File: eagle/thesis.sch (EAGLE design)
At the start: 13 parts

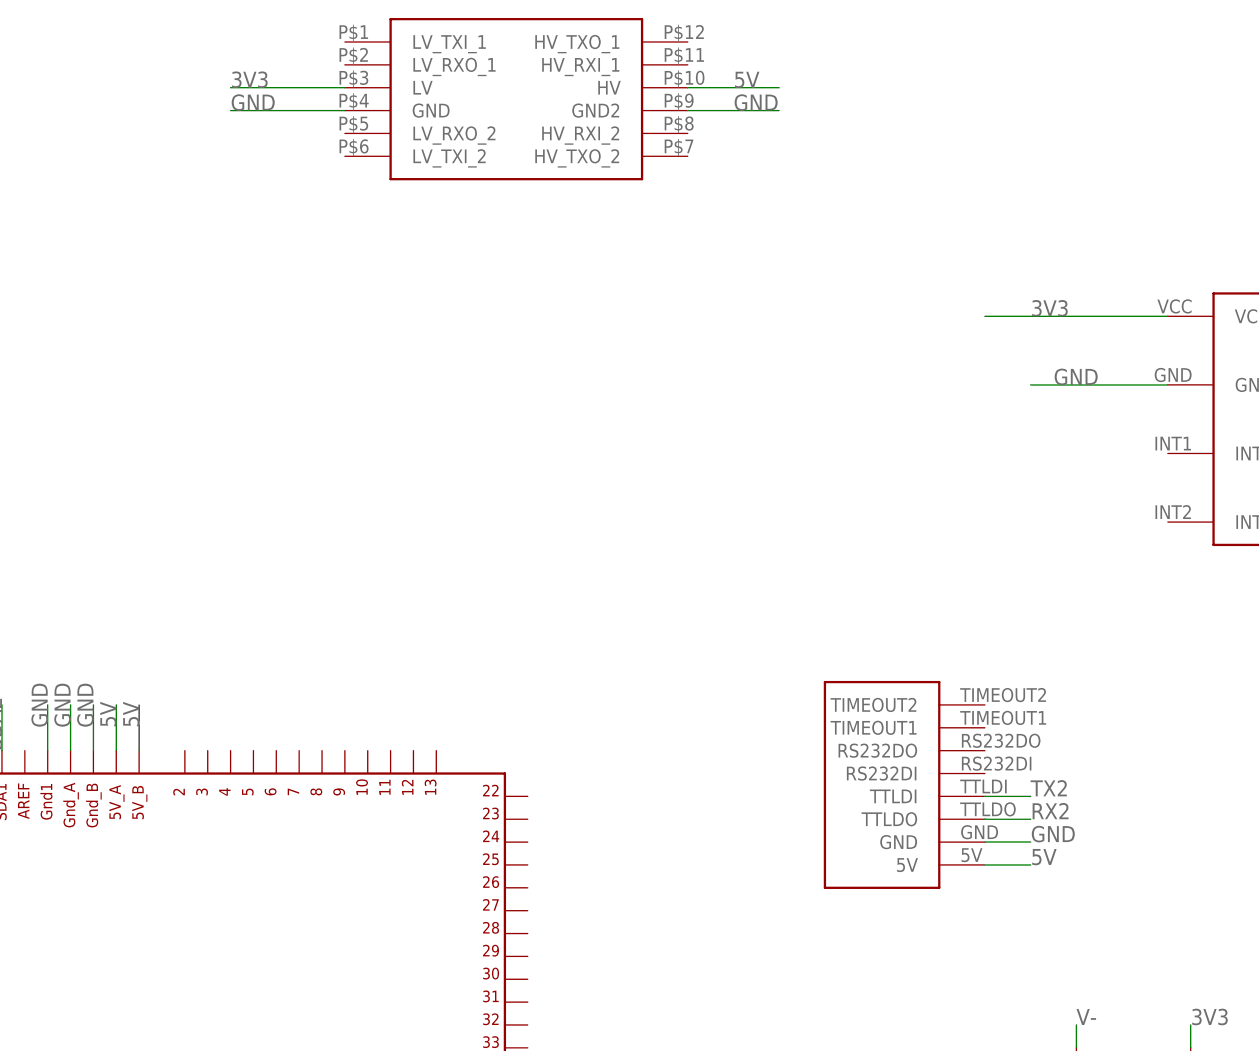
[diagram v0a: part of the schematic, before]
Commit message: added smaller satellite board
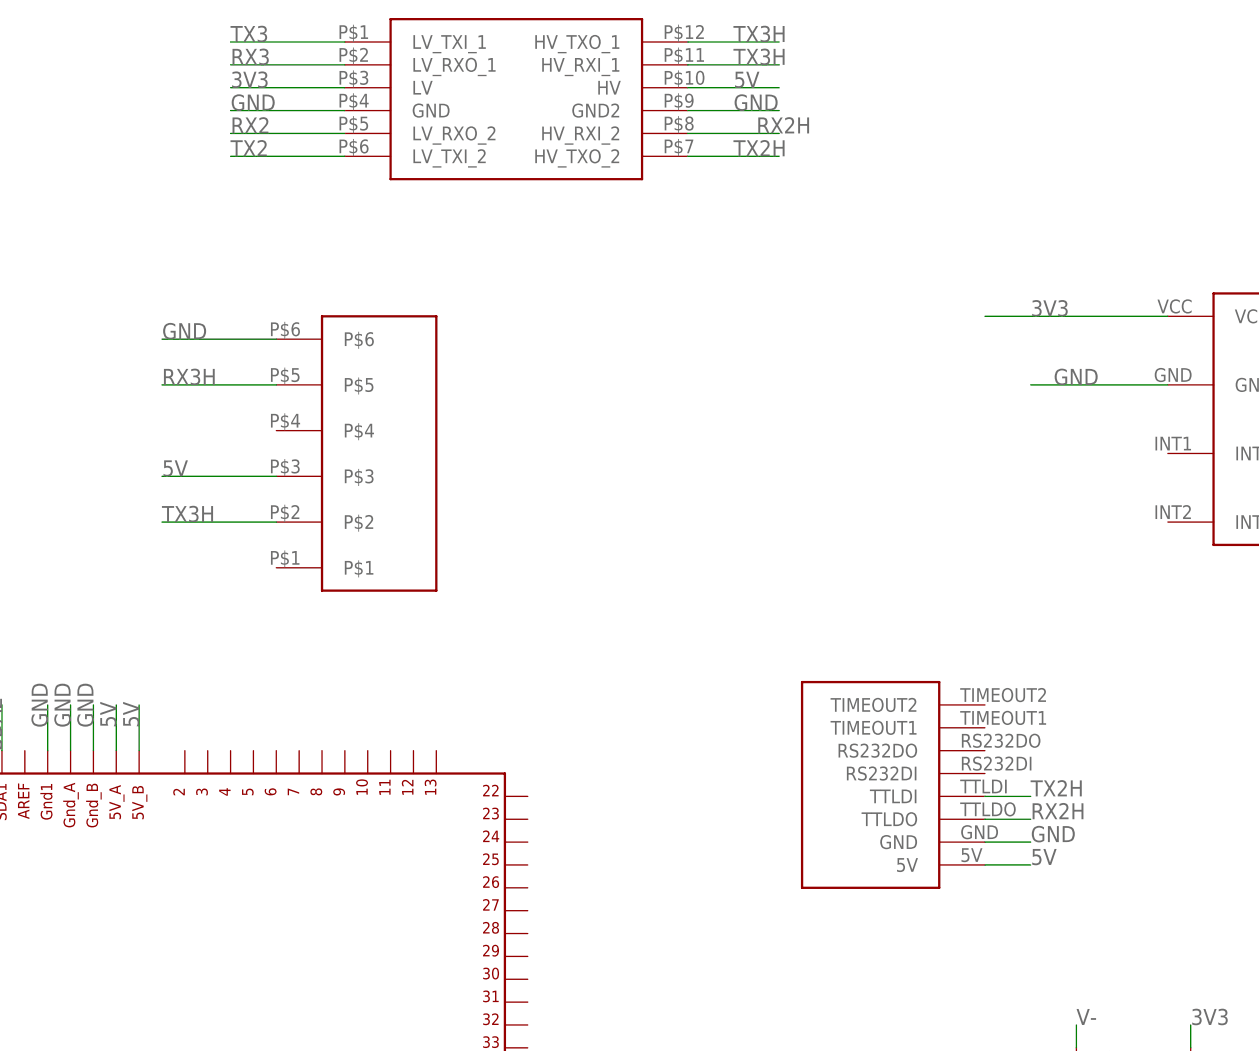
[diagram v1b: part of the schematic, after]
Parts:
- added U$8: RJ11V, RJ11V:RJ11V
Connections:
- new net RX2H: U$2.HV_RXI_2, U$6.TTLDO
- new net RX3H: U$8.P$5
- new net TX2H: U$2.HV_TXO_2, U$6.TTLDI
- new net TX3H: U$2.HV_RXI_1, U$2.HV_TXO_1, U$8.P$2
- net 5V: now also U$8.P$3
- net GND: now also U$8.P$6
- net RX2: now also U$2.LV_RXO_2; no longer U$6.TTLDO
- net RX3: now also U$2.LV_RXO_1
- net TX2: now also U$2.LV_TXI_2; no longer U$6.TTLDI
- net TX3: now also U$2.LV_TXI_1

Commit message: routed thesis board
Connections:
- new net D52: U$1.52
- new net D53: U$1.53
- net ACCELCS: now also U$1.8; no longer U$1.53
- net GND: no longer U$1.GND_DEBUG
- net RX3H: now also U$2.HV_RXI_1
- net SDCS: now also U$1.9; no longer U$1.52
- net TX3H: no longer U$2.HV_RXI_1
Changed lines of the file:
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@@
-</segment>
-<segment>
-<pinref part="U$1" gate="G$1" pin="GND_DEBUG"/>
-<wire x1="-2.54" y1="25.4" x2="-10.16" y2="25.4" width="0.1524" layer="91"/>
-<label x="-10.16" y="25.4" size="1.778" layer="95"/>
 </segment>
 <segment>
@@
 </segment>
 <segment>
+<pinref part="U$1" gate="G$1" pin="9"/>
+<wire x1="48.26" y1="93.98" x2="48.26" y2="86.36" width="0.1524" layer="91"/>
+<label x="48.26" y="88.9" size="1.778" layer="95" rot="R90"/>
+</segment>
+</net>
+<net name="ACCELCS" class="0">
+<segment>
+<pinref part="U$4" gate="G$1" pin="CS"/>
+<wire x1="200.66" y1="111.76" x2="180.34" y2="111.76" width="0.1524" layer="91"/>
+<label x="190.5" y="111.76" size="1.778" layer="95"/>
+</segment>
+<segment>
+<pinref part="U$1" gate="G$1" pin="8"/>
+<wire x1="45.72" y1="86.36" x2="45.72" y2="93.98" width="0.1524" layer="91"/>
+<label x="45.72" y="88.9" size="1.778" layer="95" rot="R90"/>
+</segment>
+</net>
+<net name="SDA2" class="0">
+<segment>
+<pinref part="U$1" gate="G$1" pin="SDA1"/>
+<wire x1="10.16" y1="86.36" x2="10.16" y2="91.44" width="0.1524" layer="91"/>
+<label x="10.16" y="86.36" size="1.778" layer="95" rot="R90"/>
+</segment>
+<segment>
+<pinref part="U$1" gate="G$1" pin="SDA"/>
+<wire x1="-10.16" y1="60.96" x2="-2.54" y2="60.96" width="0.1524" layer="91"/>
+<label x="-10.16" y="60.96" size="1.778" layer="95"/>
+</segment>
+<segment>
+<pinref part="U$7" gate="G$1" pin="SDA"/>
+<wire x1="190.5" y1="71.12" x2="203.2" y2="71.12" width="0.1524" layer="91"/>
+<label x="198.12" y="71.12" size="1.778" layer="95"/>
+</segment>
+</net>
+<net name="RX3H" class="0">
+<segment>
+<pinref part="U$8" gate="G$1" pin="P$5"/>
+<wire x1="27.94" y1="127" x2="40.64" y2="127" width="0.1524" layer="91"/>
+<label x="27.94" y="127" size="1.778" layer="95"/>
+</segment>
+<segment>
+<pinref part="U$2" gate="G$1" pin="HV_RXI_1"/>
+<wire x1="86.36" y1="162.56" x2="96.52" y2="162.56" width="0.1524" layer="91"/>
+<label x="91.44" y="162.56" size="1.778" layer="95"/>
+</segment>
+</net>
+<net name="TX3H" class="0">
+<segment>
+<pinref part="U$8" gate="G$1" pin="P$2"/>
+<wire x1="40.64" y1="111.76" x2="27.94" y2="111.76" width="0.1524" layer="91"/>
+<label x="27.94" y="111.76" size="1.778" layer="95"/>
+</segment>
+<segment>
+<pinref part="U$2" gate="G$1" pin="HV_TXO_1"/>
+<wire x1="86.36" y1="165.1" x2="96.52" y2="165.1" width="0.1524" layer="91"/>
+<label x="91.44" y="165.1" size="1.778" layer="95"/>
+</segment>
+</net>
+<net name="RX2H" class="0">
+<segment>
+<pinref part="U$2" gate="G$1" pin="HV_RXI_2"/>
+<wire x1="96.52" y1="154.94" x2="86.36" y2="154.94" width="0.1524" layer="91"/>
+<label x="93.98" y="154.94" size="1.778" layer="95"/>
+</segment>
+<segment>
+<pinref part="U$6" gate="G$1" pin="TTLDO"/>
+<wire x1="119.38" y1="78.74" x2="124.46" y2="78.74" width="0.1524" layer="91"/>
+<label x="124.46" y="78.74" size="1.778" layer="95"/>
+</segment>
+</net>
+<net name="TX2H" class="0">
+<segment>
+<pinref part="U$2" gate="G$1" pin="HV_TXO_2"/>
+<wire x1="96.52" y1="152.4" x2="86.36" y2="152.4" width="0.1524" layer="91"/>
+<label x="91.44" y="152.4" size="1.778" layer="95"/>
+</segment>
+<segment>
+<pinref part="U$6" gate="G$1" pin="TTLDI"/>
+<wire x1="124.46" y1="81.28" x2="119.38" y2="81.28" width="0.1524" layer="91"/>
+<label x="124.46" y="81.28" size="1.778" layer="95"/>
+</segment>
+</net>
+<net name="D52" class="0">
+<segment>
 <pinref part="U$1" gate="G$1" pin="52"/>
 <wire x1="68.58" y1="5.08" x2="71.12" y2="5.08" width="0.1524" layer="91"/>
@@
 </segment>
 </net>
-<net name="ACCELCS" class="0">
-<segment>
-<pinref part="U$4" gate="G$1" pin="CS"/>
-<wire x1="200.66" y1="111.76" x2="180.34" y2="111.76" width="0.1524" layer="91"/>
-<label x="190.5" y="111.76" size="1.778" layer="95"/>
-</segment>
+<net name="D53" class="0">
 <segment>
 <pinref part="U$1" gate="G$1" pin="53"/>
@@
 </segment>
 </net>
-<net name="SDA2" class="0">
-<segment>
-<pinref part="U$1" gate="G$1" pin="SDA1"/>
-<wire x1="10.16" y1="86.36" x2="10.16" y2="91.44" width="0.1524" layer="91"/>
-<label x="10.16" y="86.36" size="1.778" layer="95" rot="R90"/>
-</segment>
-<segment>
-<pinref part="U$1" gate="G$1" pin="SDA"/>
-<wire x1="-10.16" y1="60.96" x2="-2.54" y2="60.96" width="0.1524" layer="91"/>
-<label x="-10.16" y="60.96" size="1.778" layer="95"/>
-</segment>
-<segment>
-<pinref part="U$7" gate="G$1" pin="SDA"/>
-<wire x1="190.5" y1="71.12" x2="203.2" y2="71.12" width="0.1524" layer="91"/>
-<label x="198.12" y="71.12" size="1.778" layer="95"/>
-</segment>
-</net>
-<net name="RX3H" class="0">
-<segment>
-<pinref part="U$8" gate="G$1" pin="P$5"/>
-<wire x1="27.94" y1="127" x2="40.64" y2="127" width="0.1524" layer="91"/>
-<label x="27.94" y="127" size="1.778" layer="95"/>
-</segment>
-</net>
-<net name="TX3H" class="0">
-<segment>
-<pinref part="U$8" gate="G$1" pin="P$2"/>
-<wire x1="40.64" y1="111.76" x2="27.94" y2="111.76" width="0.1524" layer="91"/>
-<label x="27.94" y="111.76" size="1.778" layer="95"/>
-</segment>
-<segment>
-<pinref part="U$2" gate="G$1" pin="HV_TXO_1"/>
-<wire x1="86.36" y1="165.1" x2="96.52" y2="165.1" width="0.1524" layer="91"/>
-<label x="91.44" y="165.1" size="1.778" layer="95"/>
-</segment>
-<segment>
-<pinref part="U$2" gate="G$1" pin="HV_RXI_1"/>
-<wire x1="86.36" y1="162.56" x2="96.52" y2="162.56" width="0.1524" layer="91"/>
-<label x="91.44" y="162.56" size="1.778" layer="95"/>
-</segment>
-</net>
-<net name="RX2H" class="0">
-<segment>
-<pinref part="U$2" gate="G$1" pin="HV_RXI_2"/>
-<wire x1="96.52" y1="154.94" x2="86.36" y2="154.94" width="0.1524" layer="91"/>
-<label x="93.98" y="154.94" size="1.778" layer="95"/>
-</segment>
-<segment>
-<pinref part="U$6" gate="G$1" pin="TTLDO"/>
-<wire x1="119.38" y1="78.74" x2="124.46" y2="78.74" width="0.1524" layer="91"/>
-<label x="124.46" y="78.74" size="1.778" layer="95"/>
-</segment>
-</net>
-<net name="TX2H" class="0">
-<segment>
-<pinref part="U$2" gate="G$1" pin="HV_TXO_2"/>
-<wire x1="96.52" y1="152.4" x2="86.36" y2="152.4" width="0.1524" layer="91"/>
-<label x="91.44" y="152.4" size="1.778" layer="95"/>
-</segment>
-<segment>
-<pinref part="U$6" gate="G$1" pin="TTLDI"/>
-<wire x1="124.46" y1="81.28" x2="119.38" y2="81.28" width="0.1524" layer="91"/>
-<label x="124.46" y="81.28" size="1.778" layer="95"/>
-</segment>
-</net>

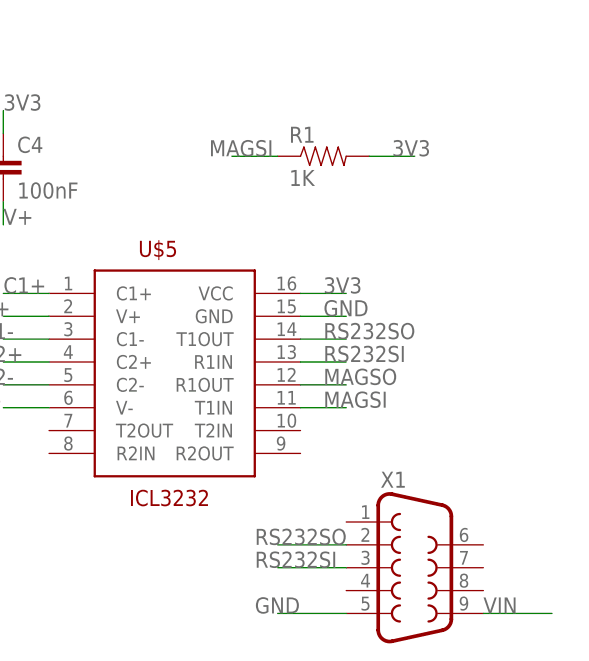
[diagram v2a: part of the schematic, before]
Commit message: modified eagle files, should be ready to order
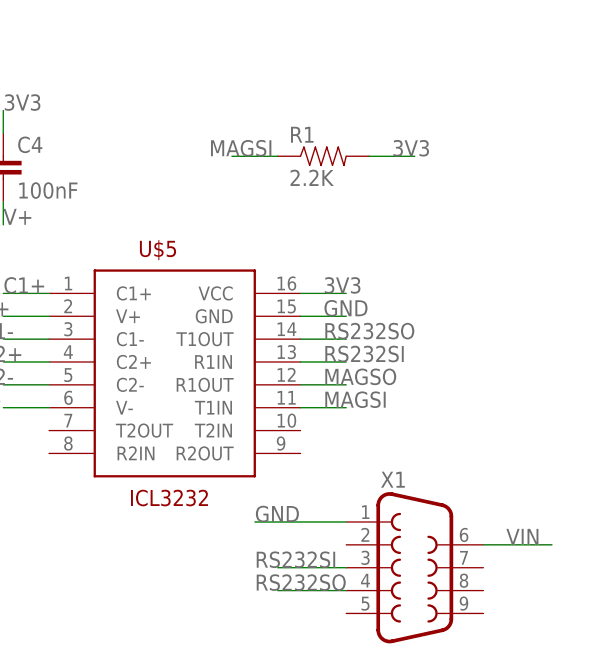
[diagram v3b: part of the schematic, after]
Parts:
- R1: value 1K -> 2.2K
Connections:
- net GND: now also X1.1; no longer X1.5
- net RS232SO: now also X1.4; no longer X1.2
- net VIN: now also X1.6; no longer X1.9
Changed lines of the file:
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@@
 <part name="C3" library="SparkFun-Passives" deviceset="CAP" device="KIT" value="100nF"/>
 <part name="C4" library="SparkFun-Passives" deviceset="CAP" device="KIT" value="100nF"/>
-<part name="R1" library="SparkFun-Resistors" deviceset="RESISTOR" device="AXIAL-0.3" value="1K"/>
+<part name="R1" library="SparkFun-Resistors" deviceset="RESISTOR" device="AXIAL-0.3" value="2.2K"/>
 <part name="U$8" library="RJ11V" deviceset="RJ11V" device=""/>
 </parts>
@@
 </segment>
 <segment>
-<pinref part="X1" gate="G$1" pin="9"/>
-<wire x1="203.2" y1="0" x2="195.58" y2="0" width="0.1524" layer="91"/>
-<label x="195.58" y="0" size="1.778" layer="95"/>
+<pinref part="X1" gate="G$1" pin="6"/>
+<wire x1="195.58" y1="7.62" x2="203.2" y2="7.62" width="0.1524" layer="91"/>
+<label x="198.12" y="7.62" size="1.778" layer="95"/>
 </segment>
 </net>
@@
 </segment>
 <segment>
-<pinref part="X1" gate="G$1" pin="5"/>
-<wire x1="180.34" y1="0" x2="172.72" y2="0" width="0.1524" layer="91"/>
-<label x="170.18" y="0" size="1.778" layer="95"/>
-</segment>
-<segment>
 <pinref part="U$3" gate="G$1" pin="GND"/>
 <wire x1="-38.1" y1="114.3" x2="-27.94" y2="114.3" width="0.1524" layer="91"/>
@@
 <label x="27.94" y="132.08" size="1.778" layer="95"/>
 </segment>
+<segment>
+<pinref part="X1" gate="G$1" pin="1"/>
+<wire x1="180.34" y1="10.16" x2="170.18" y2="10.16" width="0.1524" layer="91"/>
+<label x="170.18" y="10.16" size="1.778" layer="95"/>
+</segment>
 </net>
 <net name="V-" class="0">
@@
 </segment>
 <segment>
-<pinref part="X1" gate="G$1" pin="2"/>
-<wire x1="180.34" y1="7.62" x2="172.72" y2="7.62" width="0.1524" layer="91"/>
-<label x="170.18" y="7.62" size="1.778" layer="95"/>
-</segment>
-</net>
+<pinref part="X1" gate="G$1" pin="4"/>
+<wire x1="180.34" y1="2.54" x2="172.72" y2="2.54" width="0.1524" layer="91"/>
+<label x="170.18" y="2.54" size="1.778" layer="95"/>
+</segment>
+</net>

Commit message: modified eagle boards, ordered them.
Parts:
- renumbered U$5 to MAX3232
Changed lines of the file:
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@@
 <part name="C1" library="SparkFun-Passives" deviceset="CAP" device="KIT" value="100nF"/>
 <part name="C2" library="SparkFun-Passives" deviceset="CAP" device="KIT" value="100nF"/>
-<part name="U$5" library="SparkFun-DigitalIC" deviceset="ICL3232" device=""/>
+<part name="MAX3232" library="SparkFun-DigitalIC" deviceset="ICL3232" device=""/>
 <part name="C3" library="SparkFun-Passives" deviceset="CAP" device="KIT" value="100nF"/>
 <part name="C4" library="SparkFun-Passives" deviceset="CAP" device="KIT" value="100nF"/>
@@
 <instance part="U$7" gate="G$1" x="162.56" y="71.12"/>
 <instance part="U$3" gate="G$1" x="-22.86" y="104.14"/>
-<instance part="X1" gate="G$1" x="187.96" y="5.08"/>
+<instance part="X1" gate="G$1" x="187.96" y="5.08" smashed="yes">
+<attribute name="VALUE" x="184.15" y="-5.715" size="1.778" layer="96"/>
+<attribute name="NAME" x="184.15" y="13.97" size="1.778" layer="95"/>
+</instance>
 <instance part="C1" gate="G$1" x="121.92" y="33.02"/>
 <instance part="C2" gate="G$1" x="124.46" y="15.24"/>
-<instance part="U$5" gate="G$1" x="160.02" y="27.94"/>
+<instance part="MAX3232" gate="G$1" x="160.02" y="27.94"/>
 <instance part="C3" gate="G$1" x="129.54" y="48.26"/>
 <instance part="C4" gate="G$1" x="142.24" y="48.26"/>
@@
 </segment>
 <segment>
-<pinref part="U$5" gate="G$1" pin="VCC"/>
+<pinref part="MAX3232" gate="G$1" pin="VCC"/>
 <wire x1="180.34" y1="35.56" x2="175.26" y2="35.56" width="0.1524" layer="91"/>
 <label x="177.8" y="35.56" size="1.778" layer="95"/>
@@
 </segment>
 <segment>
-<pinref part="U$5" gate="G$1" pin="GND"/>
+<pinref part="MAX3232" gate="G$1" pin="GND"/>
 <wire x1="180.34" y1="33.02" x2="175.26" y2="33.02" width="0.1524" layer="91"/>
 <label x="177.8" y="33.02" size="1.778" layer="95"/>
@@
 <net name="V-" class="0">
 <segment>
-<pinref part="U$5" gate="G$1" pin="V-"/>
+<pinref part="MAX3232" gate="G$1" pin="V-"/>
 <wire x1="142.24" y1="22.86" x2="147.32" y2="22.86" width="0.1524" layer="91"/>
 <label x="139.7" y="22.86" size="1.778" layer="95"/>
@@
 </segment>
 <segment>
-<pinref part="U$5" gate="G$1" pin="C1+"/>
+<pinref part="MAX3232" gate="G$1" pin="C1+"/>
 <wire x1="147.32" y1="35.56" x2="142.24" y2="35.56" width="0.1524" layer="91"/>
 <label x="142.24" y="35.56" size="1.778" layer="95"/>
@@
 </segment>
 <segment>
-<pinref part="U$5" gate="G$1" pin="C1-"/>
+<pinref part="MAX3232" gate="G$1" pin="C1-"/>
 <wire x1="142.24" y1="30.48" x2="147.32" y2="30.48" width="0.1524" layer="91"/>
 <label x="139.7" y="30.48" size="1.778" layer="95"/>
@@
 </segment>
 <segment>
-<pinref part="U$5" gate="G$1" pin="C2+"/>
+<pinref part="MAX3232" gate="G$1" pin="C2+"/>
 <wire x1="142.24" y1="27.94" x2="147.32" y2="27.94" width="0.1524" layer="91"/>
 <label x="139.7" y="27.94" size="1.778" layer="95"/>
@@
 </segment>
 <segment>
-<pinref part="U$5" gate="G$1" pin="C2-"/>
+<pinref part="MAX3232" gate="G$1" pin="C2-"/>
 <wire x1="142.24" y1="25.4" x2="147.32" y2="25.4" width="0.1524" layer="91"/>
 <label x="139.7" y="25.4" size="1.778" layer="95"/>
@@
 <net name="V+" class="0">
 <segment>
-<pinref part="U$5" gate="G$1" pin="V+"/>
+<pinref part="MAX3232" gate="G$1" pin="V+"/>
 <wire x1="147.32" y1="33.02" x2="142.24" y2="33.02" width="0.1524" layer="91"/>
 <label x="139.7" y="33.02" size="1.778" layer="95"/>
@@
 <net name="RS232SO" class="0">
 <segment>
-<pinref part="U$5" gate="G$1" pin="T1OUT"/>
+<pinref part="MAX3232" gate="G$1" pin="T1OUT"/>
 <wire x1="175.26" y1="30.48" x2="180.34" y2="30.48" width="0.1524" layer="91"/>
 <label x="177.8" y="30.48" size="1.778" layer="95"/>
@@
 <net name="RS232SI" class="0">
 <segment>
-<pinref part="U$5" gate="G$1" pin="R1IN"/>
+<pinref part="MAX3232" gate="G$1" pin="R1IN"/>
 <wire x1="175.26" y1="27.94" x2="180.34" y2="27.94" width="0.1524" layer="91"/>
 <label x="177.8" y="27.94" size="1.778" layer="95"/>
@@
 <net name="MAGSI" class="0">
 <segment>
-<pinref part="U$5" gate="G$1" pin="T1IN"/>
+<pinref part="MAX3232" gate="G$1" pin="T1IN"/>
 <wire x1="175.26" y1="22.86" x2="180.34" y2="22.86" width="0.1524" layer="91"/>
 <label x="177.8" y="22.86" size="1.778" layer="95"/>
@@
 <net name="MAGSO" class="0">
 <segment>
-<pinref part="U$5" gate="G$1" pin="R1OUT"/>
+<pinref part="MAX3232" gate="G$1" pin="R1OUT"/>
 <wire x1="175.26" y1="25.4" x2="180.34" y2="25.4" width="0.1524" layer="91"/>
 <label x="177.8" y="25.4" size="1.778" layer="95"/>
